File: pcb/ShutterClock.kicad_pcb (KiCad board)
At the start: 2 copper layers, 100 x 88 mm, 58 parts, among them J1 BATTERY 12V, J2 CAMERA EP-5B, J3 3.5mm RELEASE, Q1 2SJ334 REV, Q2 2SJ334 CAM, Q3 2SK4017, Q5 2SJ334 KA, Q6 2SK4017, Q7 2SK4017 KA, SW1 TEST, U1 NJW4181U3-33B, U2 MBC2596-01 9.4V, U3 PC817 SHUTTER, U4 PC817 AF

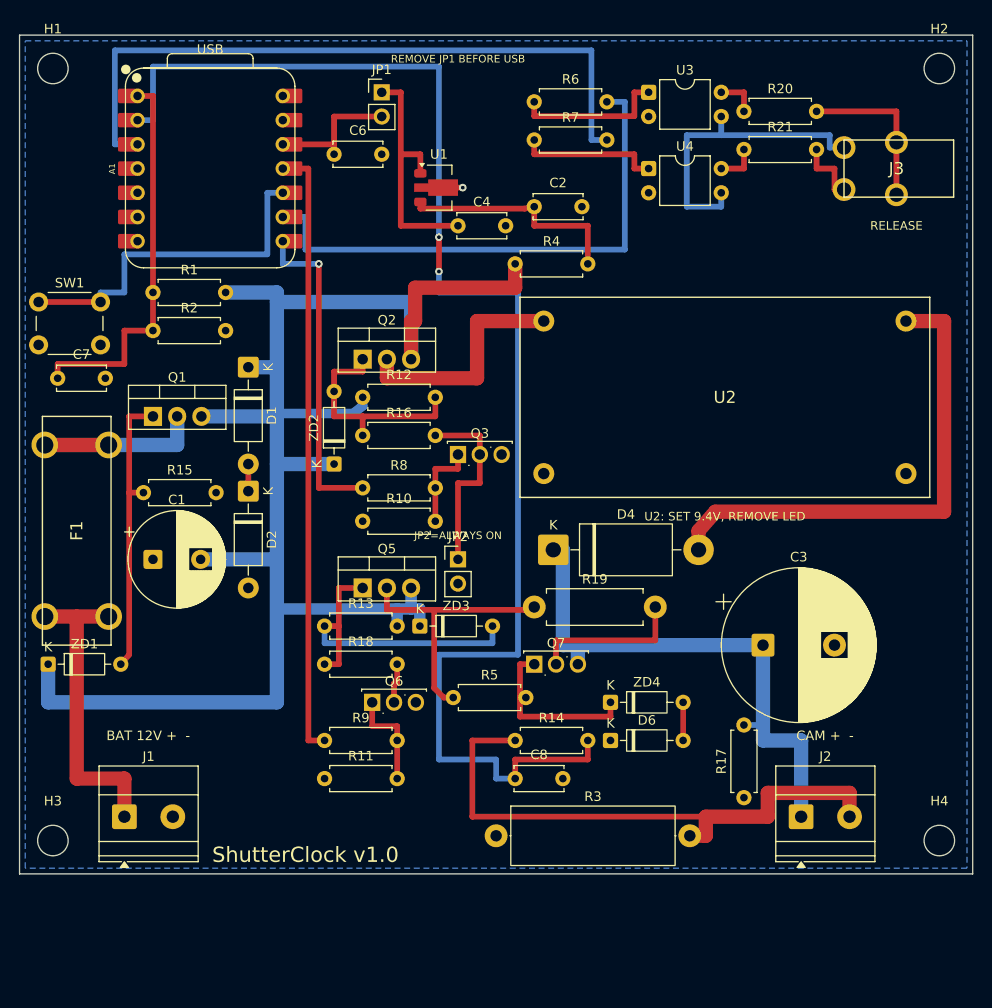
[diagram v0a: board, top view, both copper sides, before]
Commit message: PCB v1.1: fix C1 polarity nets, U2 hole pattern (40 x 17.5 mm), F1 clip pins along the fuse axis (7.0 mm); ZD1 moved; DRC clean, gerbers, renders, placement map; spec v0.16
Co-Authored-By: Claude Fable 5.1 <noreply@anthropic.com>
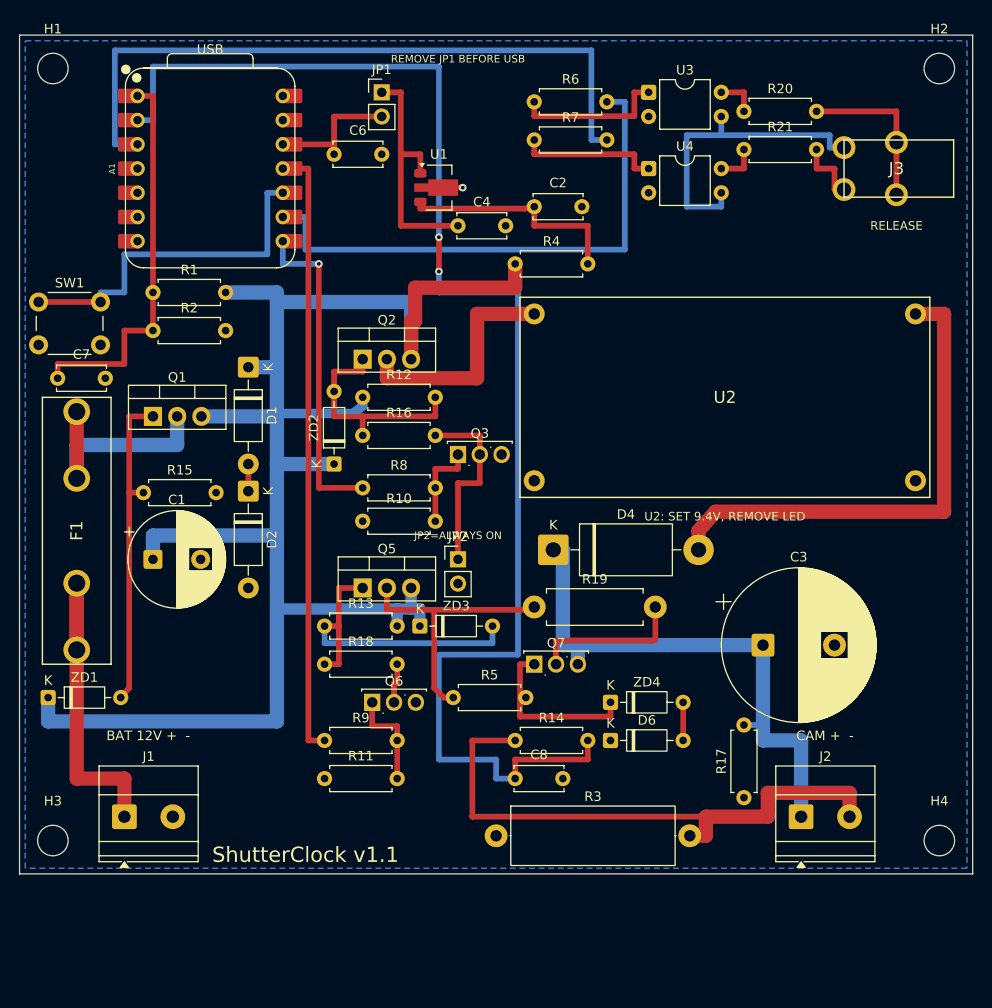
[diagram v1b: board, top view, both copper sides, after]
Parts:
- moved ZD1 3.50 mm to (3.00, 69.5)
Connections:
- C1 pad 1: GND -> VIN
- C1 pad 2: VIN -> GND
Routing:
- net VIN: track 173.3 -> 181.3 mm
- net F_OUT: track 16.9 -> 24.0 mm
- net BAT_RAW: track 32.7 -> 36.5 mm
- net Q1_G: track 30.3 -> 33.8 mm
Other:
- board text added: "ShutterClock v1.1"
- board text removed: "ShutterClock v1.0"

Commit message: PCB v1.2: RX8900 RTC module + CR2032 holder + series diode on a bottom strip (100 x 100 mm), I2C on D4/D5; DRC clean, gerbers, renders, placement map; parts list, spec v0.17
Co-Authored-By: Claude Fable 5.1 <noreply@anthropic.com>
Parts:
- added BT1: CR2032, ShutterClock:CH243-2032LF, F.Cu at (58.0, 95.0)
- added D7: 1N4148, D_DO-35_SOD27_P7.62mm_Horizontal, F.Cu at (36.2, 93.6)
- added U5: AE-RX8900, ShutterClock:AE-RX8900, F.Cu at (27.0, 94.5)
- moved H3 12.0 mm to (3.50, 96.5)
- moved H4 12.0 mm to (96.5, 96.5)
- moved SW1 2.00 mm to (4.00, 28.0)
- moved ZD1 1.00 mm to (4.00, 69.5)
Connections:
- A1 pad 5: (no net) -> SDA
- A1 pad 6: (no net) -> SCL
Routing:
- net 3V3_SYS: track 14.3 -> 152.3 mm, vias 0 -> 4
- net SDA: track 0.00 -> 107.7 mm
- net SCL: track 0.00 -> 107.7 mm
- net BT_P: track 0.00 -> 14.2 mm
- net VBAT_RTC: track 0.00 -> 10.8 mm
- net GND: track 4.36 -> 14.4 mm
- net BTN: track 37.1 -> 35.1 mm
- net VIN: track 181.3 -> 180.3 mm
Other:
- board size 100 x 88 mm -> 100 x 100 mm
- board text added: "CR2032 (+ centre pin)"
- board text added: "RTC"
- board text added: "ShutterClock v1.2"
- board text removed: "ShutterClock v1.1"
